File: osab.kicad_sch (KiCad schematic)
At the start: 100 parts, among them CON1 TF-01A, CON2 PJ-3420-A-SMT, CON3 TYPE-C-31-M-12, Q1 BC847B, Q2 BC847B, SW1 PPP, SW10 RESET, SW11 Torch, SW2 VOL-, SW3 VOL+, SW4 CHAP-, SW5 CHAP+, SW6 OT/NT, SW7 BOOK-, SW8 BOOK+, SW9 BUTTON_LOCK, U1 VS1000, U2 ME6211C33M5G-N, U3 CAT25640, U4 TP4055, U5 MF5853CS, U6 PAM8302AAS, Y1 12MHz

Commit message: production: Changed JST-type connectors
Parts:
- BATTERY1, BATTERY2: value Conn_01x02 -> (none); footprint EasyEDA model -> (none); 3D-model Included in KiCad -> (none); Link https://lcsc.com/product-detail/Wire-To-Board-Wire-To-Wire-Connector_CAX-XH-2PWB_C722862.html -> https://lcsc.com/product-detail/Wire-To-Board-Wire-To-Wire-Connector_Shenzhen-Kinghelm-Elec-KH-A2001LF-2A_C2898963.html; MPN XH-2PWB -> KH-A2001LF-2A
- SPEAKER1: value Conn_01x02 -> (none); footprint EasyEDA model -> (none); 3D-model Included in KiCad -> (none); Link https://lcsc.com/product-detail/Wire-To-Board-Wire-To-Wire-Connector_CAX-XH-2PWB_C722862.html -> https://lcsc.com/product-detail/Wire-To-Board-Wire-To-Wire-Connector_Shenzhen-Kinghelm-Elec-KH-A1001LF-02A_C2688754.html; MPN XH-2PWB -> KH-A1001LF-02A
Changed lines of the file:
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@@
       (effects (font (size 1.27 1.27)) (justify left))
     )
-    (property "Value" "Conn_01x02" (id 1) (at 271.78 86.36 0)
-      (effects (font (size 1.27 1.27)) (justify left) hide)
-    )
-    (property "Footprint" "EasyEDA model" (id 2) (at 276.86 78.74 0)
-      (effects (font (size 1.27 1.27)) hide)
-    )
-    (property "Datasheet" "https://datasheet.lcsc.com/lcsc/2009131405_CAX-XH-2PWB_C722862.pdf" (id 3) (at 276.86 78.74 0)
-      (effects (font (size 1.27 1.27)) hide)
-    )
-    (property "3D-model" "Included in KiCad" (id 4) (at 276.86 78.74 0)
-      (effects (font (size 1.27 1.27)) hide)
-    )
-    (property "Link" "https://lcsc.com/product-detail/Wire-To-Board-Wire-To-Wire-Connector_CAX-XH-2PWB_C722862.html" (id 5) (at 276.86 78.74 0)
-      (effects (font (size 1.27 1.27)) hide)
-    )
-    (property "MPN" "XH-2PWB" (id 6) (at 276.86 78.74 0)
-      (effects (font (size 1.27 1.27)) hide)
-    )
-    (pin "1")
-    (pin "2")
-  )
-  (symbol (lib_id "Connector_Generic:Conn_01x02") (at 269.24 118.11 0) (unit 1)
-    (in_bom yes) (on_board yes)
-    (property "Reference" "BATTERY1" (id 0) (at 273.05 114.3 0)
-      (effects (font (size 1.27 1.27)) (justify right))
-    )
-    (property "Value" "Conn_01x02" (id 1) (at 271.272 120.6246 0)
-      (effects (font (size 1.27 1.27)) (justify left) hide)
-    )
-    (property "Footprint" "EasyEDA model" (id 2) (at 269.24 118.11 0)
-      (effects (font (size 1.27 1.27)) hide)
-    )
-    (property "Datasheet" "https://datasheet.lcsc.com/lcsc/2009131405_CAX-XH-2PWB_C722862.pdf" (id 3) (at 269.24 118.11 0)
-      (effects (font (size 1.27 1.27)) hide)
-    )
-    (property "3D-model" "Included in KiCad" (id 4) (at 269.24 118.11 0)
-      (effects (font (size 1.27 1.27)) hide)
-    )
-    (property "Link" "https://lcsc.com/product-detail/Wire-To-Board-Wire-To-Wire-Connector_CAX-XH-2PWB_C722862.html" (id 5) (at 269.24 118.11 0)
-      (effects (font (size 1.27 1.27)) hide)
-    )
-    (property "MPN" "XH-2PWB" (id 6) (at 269.24 118.11 0)
+    (property "Value" "" (id 1) (at 271.78 86.36 0)
+      (effects (font (size 1.27 1.27)) (justify left) hide)
+    )
+    (property "Footprint" "" (id 2) (at 276.86 78.74 0)
+      (effects (font (size 1.27 1.27)) hide)
+    )
+    (property "Datasheet" "https://datasheet.lcsc.com/lcsc/2106070036_Shenzhen-Kinghelm-Elec-KH-A1001LF-02A_C2688754.pdf" (id 3) (at 276.86 78.74 0)
+      (effects (font (size 1.27 1.27)) hide)
+    )
+    (property "Link" "https://lcsc.com/product-detail/Wire-To-Board-Wire-To-Wire-Connector_Shenzhen-Kinghelm-Elec-KH-A1001LF-02A_C2688754.html" (id 5) (at 276.86 78.74 0)
+      (effects (font (size 1.27 1.27)) hide)
+    )
+    (property "MPN" "KH-A1001LF-02A" (id 6) (at 276.86 78.74 0)
       (effects (font (size 1.27 1.27)) hide)
     )
@@
     (pin "1")
   )
+  (symbol (lib_id "Connector_Generic:Conn_01x02") (at 269.24 118.11 0) (unit 1)
+    (in_bom yes) (on_board yes)
+    (property "Reference" "BATTERY1" (id 0) (at 273.05 114.3 0)
+      (effects (font (size 1.27 1.27)) (justify right))
+    )
+    (property "Value" "" (id 1) (at 271.272 120.6246 0)
+      (effects (font (size 1.27 1.27)) (justify left) hide)
+    )
+    (property "Footprint" "" (id 2) (at 269.24 118.11 0)
+      (effects (font (size 1.27 1.27)) hide)
+    )
+    (property "Datasheet" "https://datasheet.lcsc.com/lcsc/2109281630_Shenzhen-Kinghelm-Elec-KH-A2001LF-2A_C2898963.pdf" (id 3) (at 269.24 118.11 0)
+      (effects (font (size 1.27 1.27)) hide)
+    )
+    (property "Link" "https://lcsc.com/product-detail/Wire-To-Board-Wire-To-Wire-Connector_Shenzhen-Kinghelm-Elec-KH-A2001LF-2A_C2898963.html" (id 5) (at 269.24 118.11 0)
+      (effects (font (size 1.27 1.27)) hide)
+    )
+    (property "MPN" "KH-A2001LF-2A" (id 6) (at 269.24 118.11 0)
+      (effects (font (size 1.27 1.27)) hide)
+    )
+    (pin "1")
+    (pin "2")
+  )
   (symbol (lib_id "Device:R") (at 135.89 176.53 0) (unit 1)
     (in_bom yes) (on_board yes)
@@
       (effects (font (size 1.27 1.27)) (justify right))
     )
-    (property "Value" "Conn_01x02" (id 1) (at 250.698 149.8346 0)
-      (effects (font (size 1.27 1.27)) (justify left) hide)
-    )
-    (property "Footprint" "EasyEDA model" (id 2) (at 252.73 147.32 0)
-      (effects (font (size 1.27 1.27)) hide)
-    )
-    (property "Datasheet" "https://datasheet.lcsc.com/lcsc/2009131405_CAX-XH-2PWB_C722862.pdf" (id 3) (at 252.73 147.32 0)
-      (effects (font (size 1.27 1.27)) hide)
-    )
-    (property "3D-model" "Included in KiCad" (id 4) (at 252.73 147.32 0)
-      (effects (font (size 1.27 1.27)) hide)
-    )
-    (property "Link" "https://lcsc.com/product-detail/Wire-To-Board-Wire-To-Wire-Connector_CAX-XH-2PWB_C722862.html" (id 5) (at 252.73 147.32 0)
-      (effects (font (size 1.27 1.27)) hide)
-    )
-    (property "MPN" "XH-2PWB" (id 6) (at 252.73 147.32 0)
+    (property "Value" "" (id 1) (at 250.698 149.8346 0)
+      (effects (font (size 1.27 1.27)) (justify left) hide)
+    )
+    (property "Footprint" "" (id 2) (at 252.73 147.32 0)
+      (effects (font (size 1.27 1.27)) hide)
+    )
+    (property "Datasheet" "https://datasheet.lcsc.com/lcsc/2109281630_Shenzhen-Kinghelm-Elec-KH-A2001LF-2A_C2898963.pdf" (id 3) (at 252.73 147.32 0)
+      (effects (font (size 1.27 1.27)) hide)
+    )
+    (property "Link" "https://lcsc.com/product-detail/Wire-To-Board-Wire-To-Wire-Connector_Shenzhen-Kinghelm-Elec-KH-A2001LF-2A_C2898963.html" (id 5) (at 252.73 147.32 0)
+      (effects (font (size 1.27 1.27)) hide)
+    )
+    (property "MPN" "KH-A2001LF-2A" (id 6) (at 252.73 147.32 0)
       (effects (font (size 1.27 1.27)) hide)
     )
@@
       (reference "#PWR0102") (unit 1) (value "GND") (footprint "")
     )
-    (path "/00000000-0000-0000-0000-00005e040a60"
-      (reference "BATTERY1") (unit 1) (value "Conn_01x02") (footprint "EasyEDA model")
+    (path "/61df73f7-33fe-4a00-b1f0-4b1808f56cd8"
+      (reference "BATTERY1") (unit 1) (value "Conn_01x02") (footprint "Connector_JST:JST_PH_B2B-PH-SM4-TB_1x02-1MP_P2.00mm_Vertical")
     )
     (path "/697c6cc9-d8aa-43e6-9910-d8f7a42cad10"
-      (reference "BATTERY2") (unit 1) (value "Conn_01x02") (footprint "EasyEDA model")
+      (reference "BATTERY2") (unit 1) (value "Conn_01x02") (footprint "Connector_JST:JST_PH_B2B-PH-SM4-TB_1x02-1MP_P2.00mm_Vertical")
     )
     (path "/00000000-0000-0000-0000-000054d41aff"
@@
     )
     (path "/00000000-0000-0000-0000-00005e03f86a"
-      (reference "SPEAKER1") (unit 1) (value "Conn_01x02") (footprint "EasyEDA model")
+      (reference "SPEAKER1") (unit 1) (value "Conn_01x02") (footprint "Connector_JST:JST_SH_BM02B-SRSS-TB_1x02-1MP_P1.00mm_Vertical")
     )
     (path "/00000000-0000-0000-0000-0000543f883c"

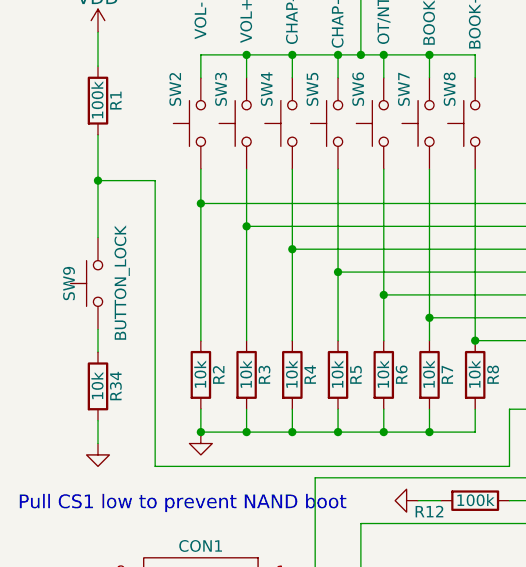
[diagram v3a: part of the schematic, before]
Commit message: production: Button lock footprint
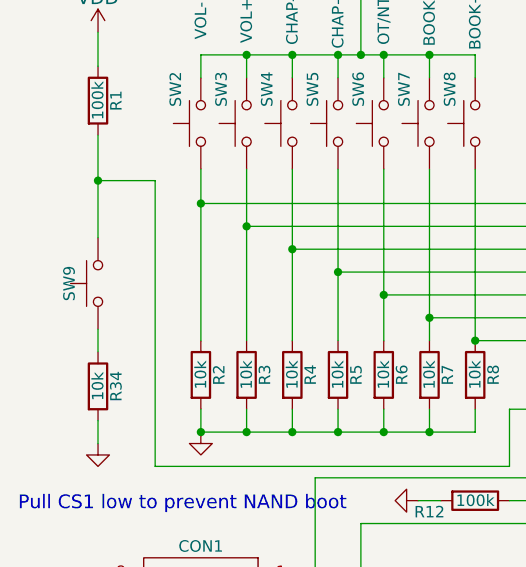
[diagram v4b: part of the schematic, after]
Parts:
- BATTERY1, BATTERY2: value (none) -> Conn_01x02; footprint (none) -> Connector_JST:JST_PH_B2B-PH-SM4-TB_1x02-1MP_P2.00mm_Vertical
- SPEAKER1: value (none) -> Conn_01x02; footprint (none) -> Connector_JST:JST_SH_BM02B-SRSS-TB_1x02-1MP_P1.00mm_Vertical
- SW9: value BUTTON_LOCK -> (none); footprint EasyEDA footprint -> (none); 3D-model NOT Included in KiCad -> (none)
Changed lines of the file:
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@@
     (in_bom yes) (on_board yes)
     (property "Reference" "SW9" (id 0) (at 18.415 77.47 0))
-    (property "Value" "BUTTON_LOCK" (id 1) (at 24.13 77.47 0))
-    (property "Footprint" "EasyEDA footprint" (id 2) (at 21.59 77.47 0)
+    (property "Value" "" (id 1) (at 24.13 77.47 0))
+    (property "Footprint" "" (id 2) (at 21.59 77.47 0)
       (effects (font (size 1.27 1.27)) hide)
     )
     (property "Datasheet" "https://datasheet.lcsc.com/lcsc/2110111730_XKB-Connectivity-XKB5858-Z-F_C780036.pdf" (id 3) (at 21.59 77.47 0)
-      (effects (font (size 1.27 1.27)) hide)
-    )
-    (property "3D-model" "NOT Included in KiCad" (id 4) (at 21.59 77.47 0)
       (effects (font (size 1.27 1.27)) hide)
     )
@@
       (effects (font (size 1.27 1.27)) (justify left))
     )
-    (property "Value" "" (id 1) (at 271.78 86.36 0)
+    (property "Value" "Conn_01x02" (id 1) (at 271.78 86.36 0)
       (effects (font (size 1.27 1.27)) (justify left) hide)
     )
-    (property "Footprint" "" (id 2) (at 276.86 78.74 0)
+    (property "Footprint" "Connector_JST:JST_SH_BM02B-SRSS-TB_1x02-1MP_P1.00mm_Vertical" (id 2) (at 276.86 78.74 0)
       (effects (font (size 1.27 1.27)) hide)
     )
@@
       (effects (font (size 1.27 1.27)) (justify right))
     )
-    (property "Value" "" (id 1) (at 271.272 120.6246 0)
+    (property "Value" "Conn_01x02" (id 1) (at 271.272 120.6246 0)
       (effects (font (size 1.27 1.27)) (justify left) hide)
     )
-    (property "Footprint" "" (id 2) (at 269.24 118.11 0)
+    (property "Footprint" "Connector_JST:JST_PH_B2B-PH-SM4-TB_1x02-1MP_P2.00mm_Vertical" (id 2) (at 269.24 118.11 0)
       (effects (font (size 1.27 1.27)) hide)
     )
@@
       (effects (font (size 1.27 1.27)) (justify right))
     )
-    (property "Value" "" (id 1) (at 250.698 149.8346 0)
+    (property "Value" "Conn_01x02" (id 1) (at 250.698 149.8346 0)
       (effects (font (size 1.27 1.27)) (justify left) hide)
     )
-    (property "Footprint" "" (id 2) (at 252.73 147.32 0)
+    (property "Footprint" "Connector_JST:JST_PH_B2B-PH-SM4-TB_1x02-1MP_P2.00mm_Vertical" (id 2) (at 252.73 147.32 0)
       (effects (font (size 1.27 1.27)) hide)
     )
@@
     )
     (path "/00000000-0000-0000-0000-00005953610d"
-      (reference "SW9") (unit 1) (value "BUTTON_LOCK") (footprint "EasyEDA footprint")
+      (reference "SW9") (unit 1) (value "BUTTON_LOCK") (footprint "OSAB:XKB5858-Z-F")
     )
     (path "/00000000-0000-0000-0000-0000543f86e6"
